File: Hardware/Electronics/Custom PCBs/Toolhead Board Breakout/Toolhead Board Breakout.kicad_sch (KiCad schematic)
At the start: 24 parts, among them J1 Conn_02x08_Odd_Even, J10 Conn_01x03, J11 Conn_01x03, J12 Conn_01x03, J13 Conn_01x02, J14 Conn_01x04, J15 Conn_01x02, J16 Conn_01x04, J17 Conn_01x02, J18 Conn_01x02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

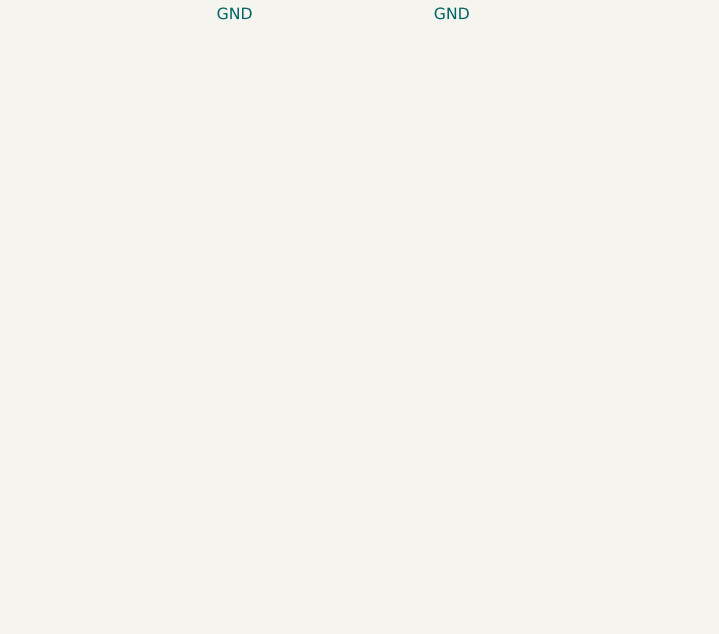
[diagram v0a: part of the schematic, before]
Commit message: updated breakout board design with added LDO's
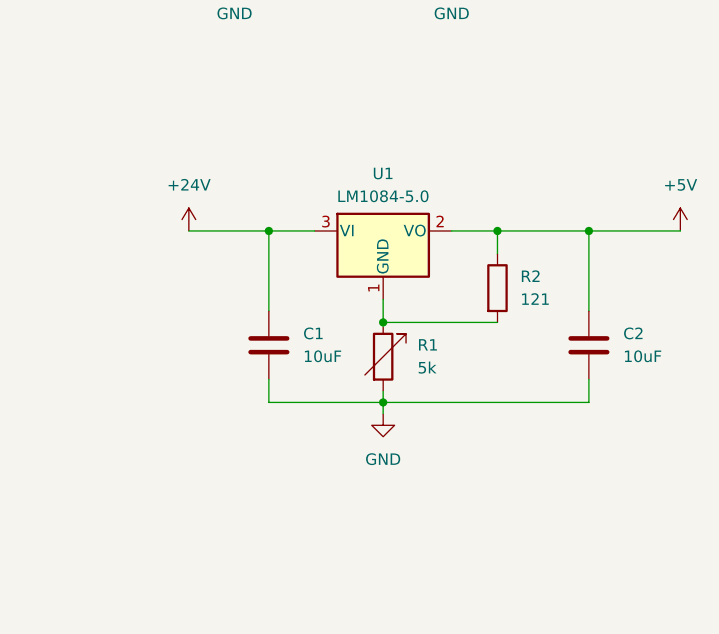
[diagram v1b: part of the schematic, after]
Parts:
- added C1, C2: 10uF, Capacitor_SMD:C_0805_2012Metric_Pad1.18x1.45mm_HandSolder, symbol Device:C
- added R1: 5k, symbol Device:R_Variable
- added R2: 121, symbol Device:R
- added U1: LM1084-5.0, symbol Regulator_Linear:LM1084-5.0
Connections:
- net +24V: now also C1.1, U1.3 (VI)
- net +5V: now also C2.1, R2.1, U1.2 (VO)
- net GND: now also C1.2, C2.2, R1.2
- new net: R1.1, R2.2, U1.1 (GND)

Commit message: updated breakout board
LDO footprint
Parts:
- U1: footprint (none) -> Package_TO_SOT_SMD:TO-263-3_TabPin2
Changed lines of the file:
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@@
 			)
 		)
-		(property "Footprint" ""
+		(property "Footprint" "Package_TO_SOT_SMD:TO-263-3_TabPin2"
 			(at 228.6 67.31 0)
 			(effects

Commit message: Finished Breakout Board
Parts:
- R1: footprint (none) -> Potentiometer_SMD:Potentiometer_Bourns_TC33X_Vertical
- R2: footprint (none) -> Resistor_SMD:R_0805_2012Metric_Pad1.20x1.40mm_HandSolder
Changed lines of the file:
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@@
 			)
 		)
-		(property "Footprint" ""
+		(property "Footprint" "Potentiometer_SMD:Potentiometer_Bourns_TC33X_Vertical"
 			(at 226.822 87.63 90)
 			(effects
@@
 			)
 		)
-		(property "Footprint" ""
+		(property "Footprint" "Resistor_SMD:R_0805_2012Metric_Pad1.20x1.40mm_HandSolder"
 			(at 239.522 80.01 90)
 			(effects

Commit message: Finish wrist motor mount and update breakout layout
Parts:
- removed J16, J19, J20: Conn_01x04, Connector_JST:JST_PH_B4B-PH-K_1x04_P2.00mm_Vertical, symbol Connector_Generic:Conn_01x04
- added C3, C4: 10uF, Capacitor_SMD:C_0805_2012Metric_Pad1.18x1.45mm_HandSolder, symbol Device:C
- added R3: 5k, Potentiometer_SMD:Potentiometer_Bourns_TC33X_Vertical, symbol Device:R_Variable
- added R4: 121, Resistor_SMD:R_0805_2012Metric_Pad1.20x1.40mm_HandSolder, symbol Device:R
- added U2: LM1084-5.0, Package_TO_SOT_SMD:TO-263-3_TabPin2, symbol Regulator_Linear:LM1084-5.0
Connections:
- net +24V: now also C3.1, U2.3 (VI)
- net +5V: no longer C2.1, J11.2 (Pin_2), J12.2 (Pin_2), J7.2 (Pin_2), J8.2 (Pin_2), R2.1, U1.2 (VO)
- net GND: now also C3.2, C4.2, R3.2
- new net: R3.1, R4.2, U2.1 (GND)
- new net 5VA: C2.1, J7.2 (Pin_2), J8.2 (Pin_2), R2.1, U1.2 (VO)
- new net 5VB: C4.1, J11.2 (Pin_2), J12.2 (Pin_2), R4.1, U2.2 (VO)
